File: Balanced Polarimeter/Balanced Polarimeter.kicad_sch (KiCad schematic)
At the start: 15 parts, among them IC1 OP27, Q1 MMPQ3904, Q2 MMPQ3904, U1 ADA4898-1YRDZ, U2 ADA4898-1YRDZ

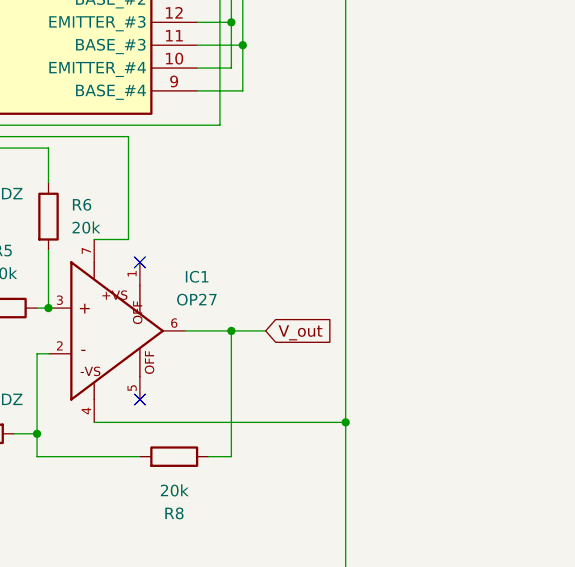
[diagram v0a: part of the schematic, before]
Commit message: Added BNC
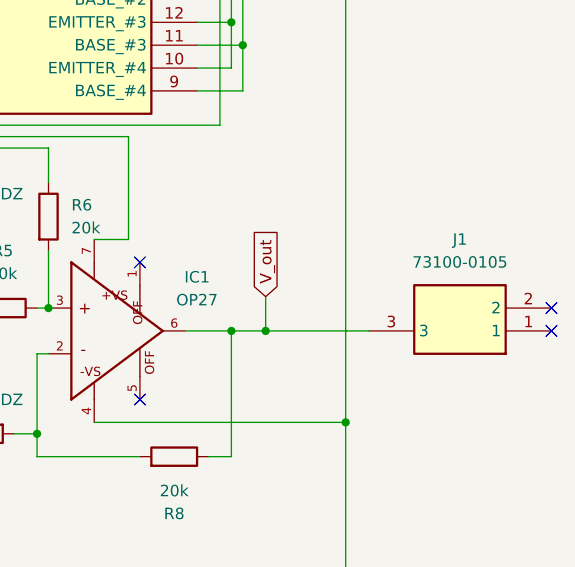
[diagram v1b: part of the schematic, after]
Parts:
- added J1: 73100-0105, 73100-0105, symbol BNC Connector:73100-0105
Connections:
- net V_out: now also J1.3
- no-connect marks 6 -> 8
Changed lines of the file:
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@@
+	)
+	(junction
+		(at 140.97 91.44)
+		(diameter 0)
+		(color 0 0 0 0)
 	)
 	(junction
@@
 	)
 	(no_connect
+		(at 172.72 91.44)
+	)
+	(no_connect
 		(at 95.25 87.63)
 	)
@@
 	)
 	(no_connect
+		(at 172.72 88.9)
+	)
+	(no_connect
 		(at 92.71 87.63)
 	)
@@
 	(wire
 		(pts
+			(xy 140.97 87.63) (xy 140.97 91.44)
+		)
+		(stroke
+			(width 0)
+			(type default)
+		)
+	)
+	(wire
+		(pts
 			(xy 76.2 48.26) (xy 73.66 48.26)
 		)
@@
 		(pts
 			(xy 133.35 135.89) (xy 138.43 135.89)
+		)
+		(stroke
+			(width 0)
+			(type default)
+		)
+	)
+	(wire
+		(pts
+			(xy 140.97 91.44) (xy 152.4 91.44)
 		)
 		(stroke
@@
 	(global_label "V_out"
 		(shape input)
-		(at 140.97 91.44 0)
+		(at 140.97 87.63 90)
 		(fields_autoplaced yes)
 		(effects
@@
 		)
 		(property "Intersheetrefs" "${INTERSHEET_REFS}"
-			(at 149.0351 91.44 0)
+			(at 140.97 79.5649 90)
 			(effects
 				(font
@@
 					(unit 1)
 				)
+			)
+		)
+	)
+	(symbol
+		(lib_id "BNC Connector:73100-0105")
+		(at 172.72 91.44 180)
+		(unit 1)
+		(exclude_from_sim no)
+		(in_bom yes)
+		(on_board yes)
+		(dnp no)
+		(fields_autoplaced yes)
+		(property "Reference" "J1"
+			(at 162.56 81.28 0)
+			(effects
+				(font
+					(size 1.27 1.27)
+				)
+			)
+		)
+		(property "Value" "73100-0105"
+			(at 162.56 83.82 0)
+			(effects
+				(font
+					(size 1.27 1.27)
+				)
+			)
+		)
+		(property "Footprint" "73100-0105"
+			(at 156.21 -3.48 0)
+			(effects
+				(font
+					(size 1.27 1.27)
+				)
+				(justify left top)
+				(hide yes)
+			)
+		)
+		(property "Datasheet" ""
+			(at 156.21 -103.48 0)
+			(effects
+				(font
+					(size 1.27 1.27)
+				)
+				(justify left top)
+				(hide yes)
+			)
+		)
+		(property "Description" "MOLEX - 73100-0105 - RF/COAXIAL, BNC JACK, R/A, 50 OHM, SOLDER"
+			(at 172.72 91.44 0)
+			(effects
+				(font
+					(size 1.27 1.27)
+				)
+				(hide yes)
+			)
+		)
+		(property "Height" ""
+			(at 156.21 -303.48 0)
+			(effects
+				(font
+					(size 1.27 1.27)
+				)
+				(justify left top)
+				(hide yes)
+			)
+		)
+		(property "Mouser Part Number" "538-73100-0105"
+			(at 156.21 -403.48 0)
+			(effects
+				(font
+					(size 1.27 1.27)
+				)
+				(justify left top)
+				(hide yes)
+			)
+		)
+		(property "Mouser Price/Stock" "https://www.mouser.co.uk/ProductDetail/Molex/73100-0105?qs=K8BHR703ZXgAHDUsVPihfA%3D%3D"
+			(at 156.21 -503.48 0)
+			(effects
+				(font
+					(size 1.27 1.27)
+				)
+				(justify left top)
+				(hide yes)
+			)
+		)
+		(property "Manufacturer_Name" "Molex"
+			(at 156.21 -603.48 0)
+			(effects
+				(font
+					(size 1.27 1.27)
+				)
+				(justify left top)
+				(hide yes)
+			)
+		)
+		(property "Manufacturer_Part_Number" "73100-0105"
+			(at 156.21 -703.48 0)
+			(effects
+				(font
+					(size 1.27 1.27)
+				)
+				(justify left top)
+				(hide yes)
+			)
+		)
+		(pin "3"
+		)
+		(pin "2"
+		)
+		(pin "1"
+		)
+		(instances
+			(project ""
+				(path "/39b6f1f8-5860-42a5-94c2-dd498265d0fe"
+					(reference "J1")
+					(unit 1)
+				)

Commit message: Updates
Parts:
- added H1, H2, H3, H4: MountingHole, MountingHole:MountingHole_2.1mm, symbol Mechanical:MountingHole
- added J2, J3: Conn_01x03_Pin, Connector_PinHeader_1.00mm:PinHeader_1x03_P1.00mm_Vertical, symbol Connector:Conn_01x03_Pin
- added J4: Conn_01x02_Pin, Connector_PinHeader_1.00mm:PinHeader_1x02_P1.00mm_Vertical, symbol Connector:Conn_01x02_Pin

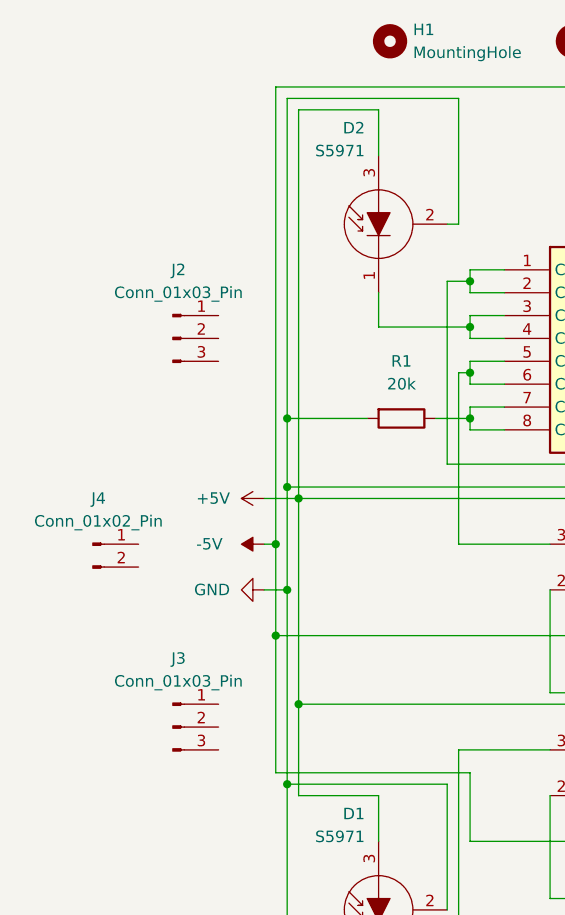
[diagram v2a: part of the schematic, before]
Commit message: Added GND Layer and 2mm Mount Holes
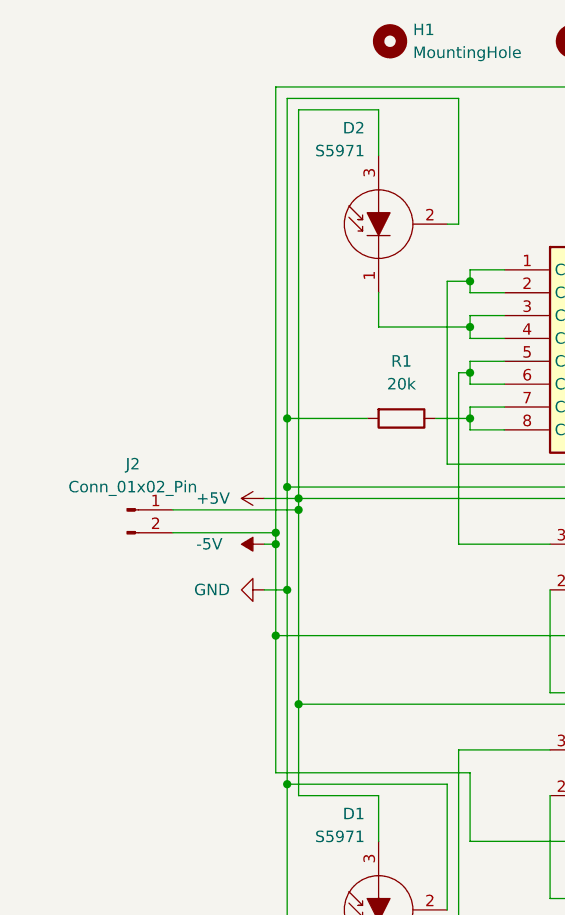
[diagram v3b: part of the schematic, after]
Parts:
- removed J2, J3: Conn_01x03_Pin, Connector_PinHeader_1.00mm:PinHeader_1x03_P1.00mm_Vertical, symbol Connector:Conn_01x03_Pin
- removed J4: Conn_01x02_Pin, Connector_PinHeader_1.00mm:PinHeader_1x02_P1.00mm_Vertical, symbol Connector:Conn_01x02_Pin
- added J2: Conn_01x02_Pin, Connector_PinHeader_1.00mm:PinHeader_1x02_P1.00mm_Vertical, symbol Connector:Conn_01x02_Pin
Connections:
- net +5V: now also J2.1 (Pin_1)
- net -5V: now also J2.2 (Pin_2)
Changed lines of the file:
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@@
 	)
 	(junction
+		(at 54.61 76.2)
+		(diameter 0)
+		(color 0 0 0 0)
+	)
+	(junction
 		(at 55.88 63.5)
 		(diameter 0)
@@
 	)
 	(junction
+		(at 57.15 73.66)
+		(diameter 0)
+		(color 0 0 0 0)
+	)
+	(junction
 		(at 76.2 63.5)
 		(diameter 0)
@@
 	(wire
 		(pts
+			(xy 57.15 73.66) (xy 57.15 95.25)
+		)
+		(stroke
+			(width 0)
+			(type default)
+		)
+	)
+	(wire
+		(pts
 			(xy 73.66 41.91) (xy 74.93 41.91)
 		)
@@
 	(wire
 		(pts
+			(xy 43.18 76.2) (xy 54.61 76.2)
+		)
+		(stroke
+			(width 0)
+			(type default)
+		)
+	)
+	(wire
+		(pts
 			(xy 137.16 123.19) (xy 137.16 133.35)
 		)
@@
 	(wire
 		(pts
+			(xy 54.61 76.2) (xy 54.61 77.47)
+		)
+		(stroke
+			(width 0)
+			(type default)
+		)
+	)
+	(wire
+		(pts
 			(xy 76.2 124.46) (xy 76.2 123.19)
 		)
@@
 	(wire
 		(pts
+			(xy 43.18 73.66) (xy 57.15 73.66)
+		)
+		(stroke
+			(width 0)
+			(type default)
+		)
+	)
+	(wire
+		(pts
 			(xy 76.2 125.73) (xy 76.2 124.46)
 		)
@@
 	(wire
 		(pts
-			(xy 57.15 72.39) (xy 57.15 95.25)
+			(xy 57.15 72.39) (xy 57.15 73.66)
 		)
 		(stroke
@@
 	(wire
 		(pts
-			(xy 54.61 26.67) (xy 54.61 77.47)
+			(xy 54.61 26.67) (xy 54.61 76.2)
 		)
 		(stroke
@@
 	)
 	(symbol
+		(lib_id "Connector:Conn_01x02_Pin")
+		(at 38.1 73.66 0)
+		(unit 1)
+		(exclude_from_sim no)
+		(in_bom yes)
+		(on_board yes)
+		(dnp no)
+		(fields_autoplaced yes)
+		(property "Reference" "J2"
+			(at 38.735 68.58 0)
+			(effects
+				(font
+					(size 1.27 1.27)
+				)
+			)
+		)
+		(property "Value" "Conn_01x02_Pin"
+			(at 38.735 71.12 0)
+			(effects
+				(font
+					(size 1.27 1.27)
+				)
+			)
+		)
+		(property "Footprint" "Connector_PinHeader_1.00mm:PinHeader_1x02_P1.00mm_Vertical"
+			(at 38.1 73.66 0)
+			(effects
+				(font
+					(size 1.27 1.27)
+				)
+				(hide yes)
+			)
+		)
+		(property "Datasheet" "~"
+			(at 38.1 73.66 0)
+			(effects
+				(font
+					(size 1.27 1.27)
+				)
+				(hide yes)
+			)
+		)
+		(property "Description" "Generic connector, single row, 01x02, script generated"
+			(at 38.1 73.66 0)
+			(effects
+				(font
+					(size 1.27 1.27)
+				)
+				(hide yes)
+			)
+		)
+		(pin "1"
+		)
+		(pin "2"
+		)
+		(instances
+			(project "Balanced Polarimeter"
+				(path "/39b6f1f8-5860-42a5-94c2-dd498265d0fe"
+					(reference "J2")
+					(unit 1)
+				)
+			)
+		)
+	)
+	(symbol
 		(lib_id "Mechanical:MountingHole")
 		(at 87.63 21.59 0)
@@
 	)
 	(symbol
-		(lib_id "Connector:Conn_01x03_Pin")
-		(at 43.18 97.79 0)
-		(unit 1)
-		(exclude_from_sim no)
-		(in_bom yes)
-		(on_board yes)
-		(dnp no)
-		(fields_autoplaced yes)
-		(property "Reference" "J3"
-			(at 43.815 90.17 0)
-			(effects
-				(font
-					(size 1.27 1.27)
-				)
-			)
-		)
-		(property "Value" "Conn_01x03_Pin"
-			(at 43.815 92.71 0)
-			(effects
-				(font
-					(size 1.27 1.27)
-				)
-			)
-		)
-		(property "Footprint" "Connector_PinHeader_1.00mm:PinHeader_1x03_P1.00mm_Vertical"
-			(at 43.18 97.79 0)
-			(effects
-				(font
-					(size 1.27 1.27)
-				)
-				(hide yes)
-			)
-		)
-		(property "Datasheet" "~"
-			(at 43.18 97.79 0)
-			(effects
-				(font
-					(size 1.27 1.27)
-				)
-				(hide yes)
-			)
-		)
-		(property "Description" "Generic connector, single row, 01x03, script generated"
-			(at 43.18 97.79 0)
-			(effects
-				(font
-					(size 1.27 1.27)
-				)
-				(hide yes)
-			)
-		)
-		(pin "1"
-		)
-		(pin "2"
-		)
-		(pin "3"
-		)
-		(instances
-			(project "Balanced Polarimeter"
-				(path "/39b6f1f8-5860-42a5-94c2-dd498265d0fe"
-					(reference "J3")
-					(unit 1)
-				)
-			)
-		)
-	)
-	(symbol
 		(lib_id "Device:R")
 		(at 116.84 78.74 0)
@@
 	)
 	(symbol
-		(lib_id "Connector:Conn_01x02_Pin")
-		(at 34.29 77.47 0)
-		(unit 1)
-		(exclude_from_sim no)
-		(in_bom yes)
-		(on_board yes)
-		(dnp no)
-		(fields_autoplaced yes)
-		(property "Reference" "J4"
-			(at 34.925 72.39 0)
-			(effects
-				(font
-					(size 1.27 1.27)
-				)
-			)
-		)
-		(property "Value" "Conn_01x02_Pin"
-			(at 34.925 74.93 0)
-			(effects
-				(font
-					(size 1.27 1.27)
-				)
-			)
-		)
-		(property "Footprint" "Connector_PinHeader_1.00mm:PinHeader_1x02_P1.00mm_Vertical"
-			(at 34.29 77.47 0)
-			(effects
-				(font
-					(size 1.27 1.27)
-				)
-				(hide yes)
-			)
-		)
-		(property "Datasheet" "~"
-			(at 34.29 77.47 0)
-			(effects
-				(font
-					(size 1.27 1.27)
-				)
-				(hide yes)
-			)
-		)
-		(property "Description" "Generic connector, single row, 01x02, script generated"
-			(at 34.29 77.47 0)
-			(effects
-				(font
-					(size 1.27 1.27)
-				)
-				(hide yes)
-			)
-		)
-		(pin "1"
-		)
-		(pin "2"
-		)
-		(instances
-			(project ""
-				(path "/39b6f1f8-5860-42a5-94c2-dd498265d0fe"
-					(reference "J4")
-					(unit 1)
-				)
-			)
-		)
-	)
-	(symbol
 		(lib_id "OP27:OP27")
 		(at 121.92 91.44 0)
@@
 					(unit 1)
 				)
-			)
-		)
-	)
-	(symbol
-		(lib_id "Connector:Conn_01x03_Pin")
-		(at 43.18 54.61 0)
-		(unit 1)
-		(exclude_from_sim no)
-		(in_bom yes)
-		(on_board yes)
-		(dnp no)
-		(fields_autoplaced yes)
-		(property "Reference" "J2"
-			(at 43.815 46.99 0)
-			(effects
-				(font
-					(size 1.27 1.27)
-				)
-			)
-		)
-		(property "Value" "Conn_01x03_Pin"
-			(at 43.815 49.53 0)
-			(effects
-				(font
-					(size 1.27 1.27)
-				)
-			)
-		)
-		(property "Footprint" "Connector_PinHeader_1.00mm:PinHeader_1x03_P1.00mm_Vertical"
-			(at 43.18 54.61 0)
-			(effects
-				(font
-					(size 1.27 1.27)
-				)
-				(hide yes)
-			)
-		)
-		(property "Datasheet" "~"
-			(at 43.18 54.61 0)
-			(effects
-				(font
-					(size 1.27 1.27)
-				)
-				(hide yes)
-			)
-		)
-		(property "Description" "Generic connector, single row, 01x03, script generated"
-			(at 43.18 54.61 0)
-			(effects
-				(font
-					(size 1.27 1.27)
-				)
-				(hide yes)
-			)
-		)
-		(pin "1"
-		)
-		(pin "2"
-		)
-		(pin "3"
-		)
-		(instances
-			(project ""
-				(path "/39b6f1f8-5860-42a5-94c2-dd498265d0fe"
-					(reference "J2")
-					(unit 1)
-				)
